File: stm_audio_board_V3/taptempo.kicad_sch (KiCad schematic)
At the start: 19 parts, among them J17 Conn_01x10_Footswitch, U13 74HC14

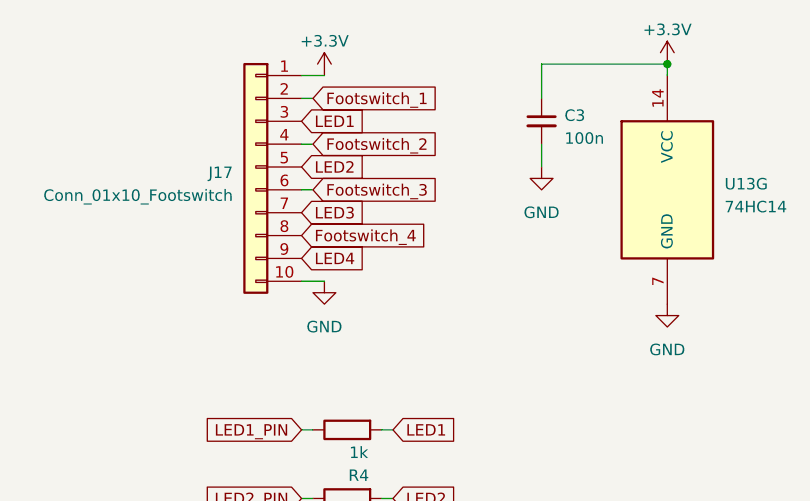
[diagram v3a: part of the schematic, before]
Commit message: added external pot, added feedback leds, added I2C between MCUs
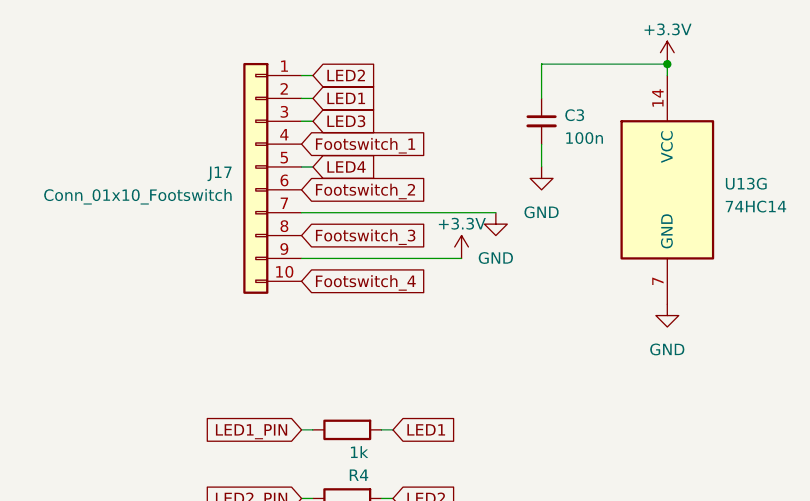
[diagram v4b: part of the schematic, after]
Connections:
- net +3.3V: now also J17.9 (Pin_9); no longer J17.1 (Pin_1)
- net Footswitch_1: now also J17.4 (Pin_4); no longer J17.2 (Pin_2)
- net Footswitch_2: now also J17.6 (Pin_6); no longer J17.4 (Pin_4)
- net Footswitch_3: now also J17.8 (Pin_8); no longer J17.6 (Pin_6)
- net Footswitch_4: now also J17.10 (Pin_10); no longer J17.8 (Pin_8)
- net GND: now also J17.7 (Pin_7); no longer J17.10 (Pin_10)
- net LED1: now also J17.2 (Pin_2); no longer J17.3 (Pin_3)
- net LED2: now also J17.1 (Pin_1); no longer J17.5 (Pin_5)
- net LED3: now also J17.3 (Pin_3); no longer J17.7 (Pin_7)
- net LED4: now also J17.5 (Pin_5); no longer J17.9 (Pin_9)

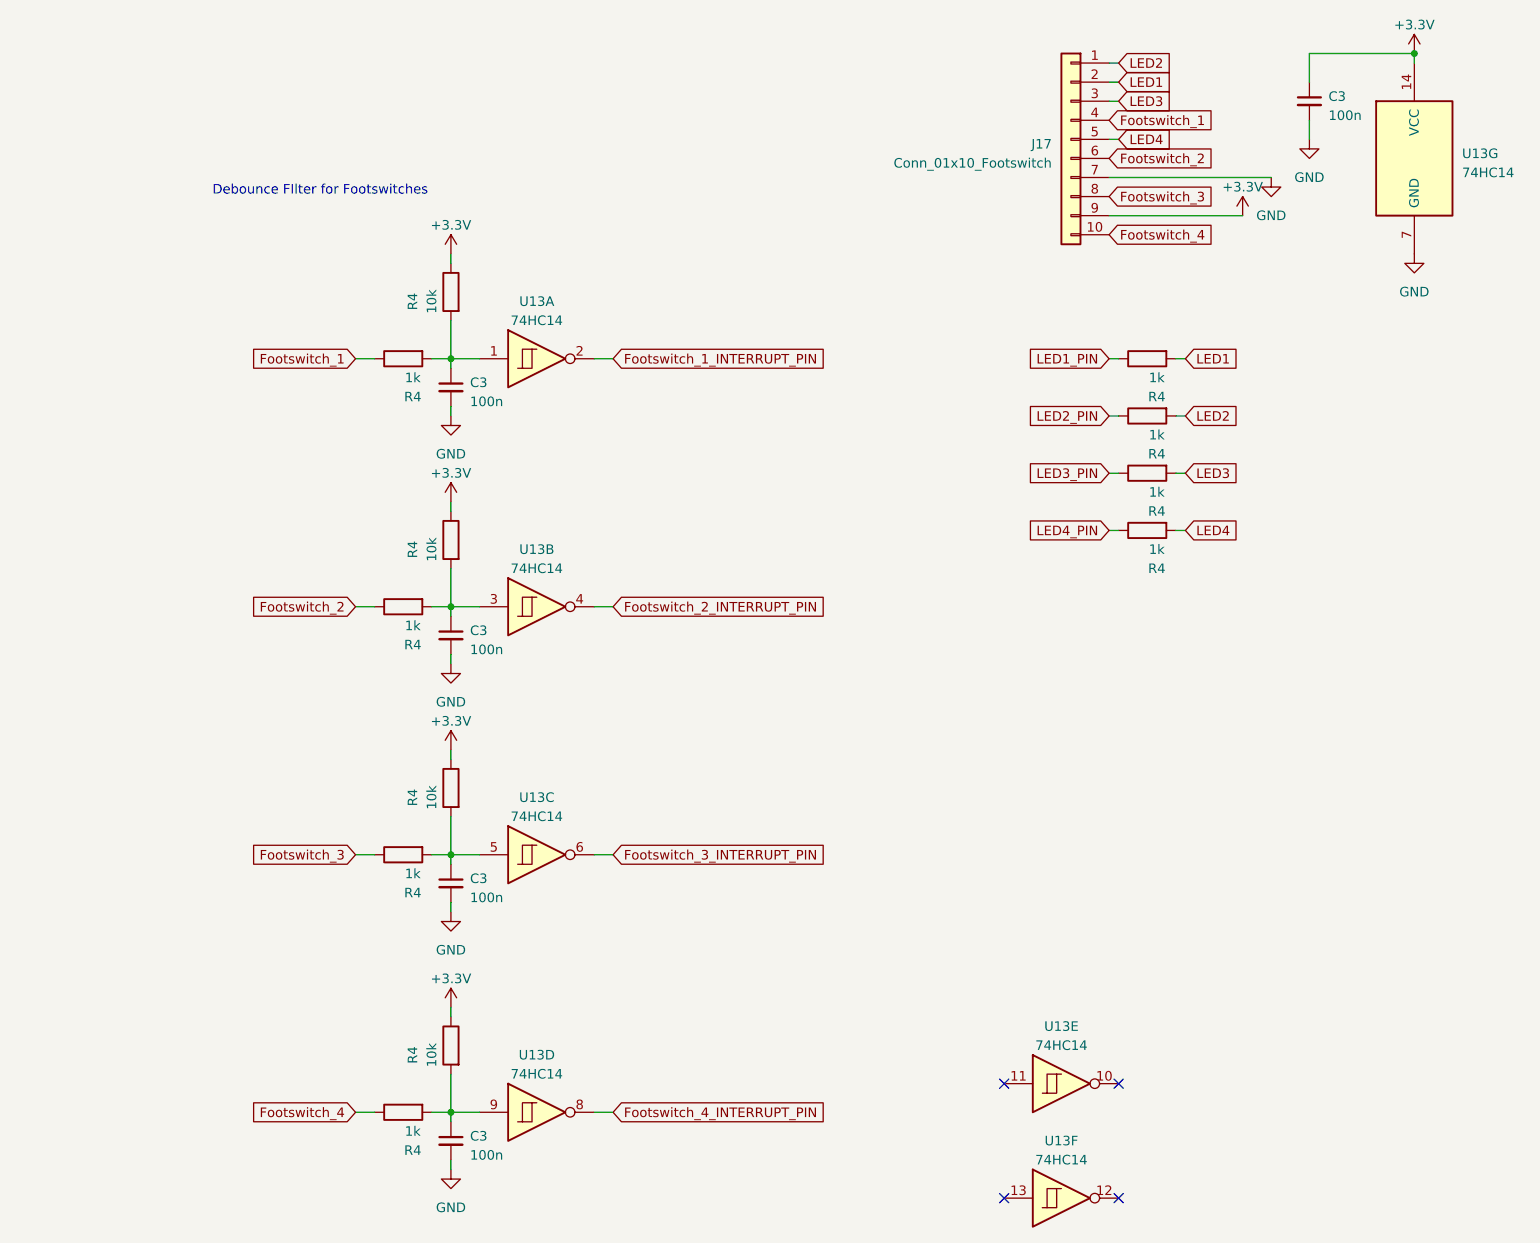
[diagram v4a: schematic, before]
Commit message: minor changes to components
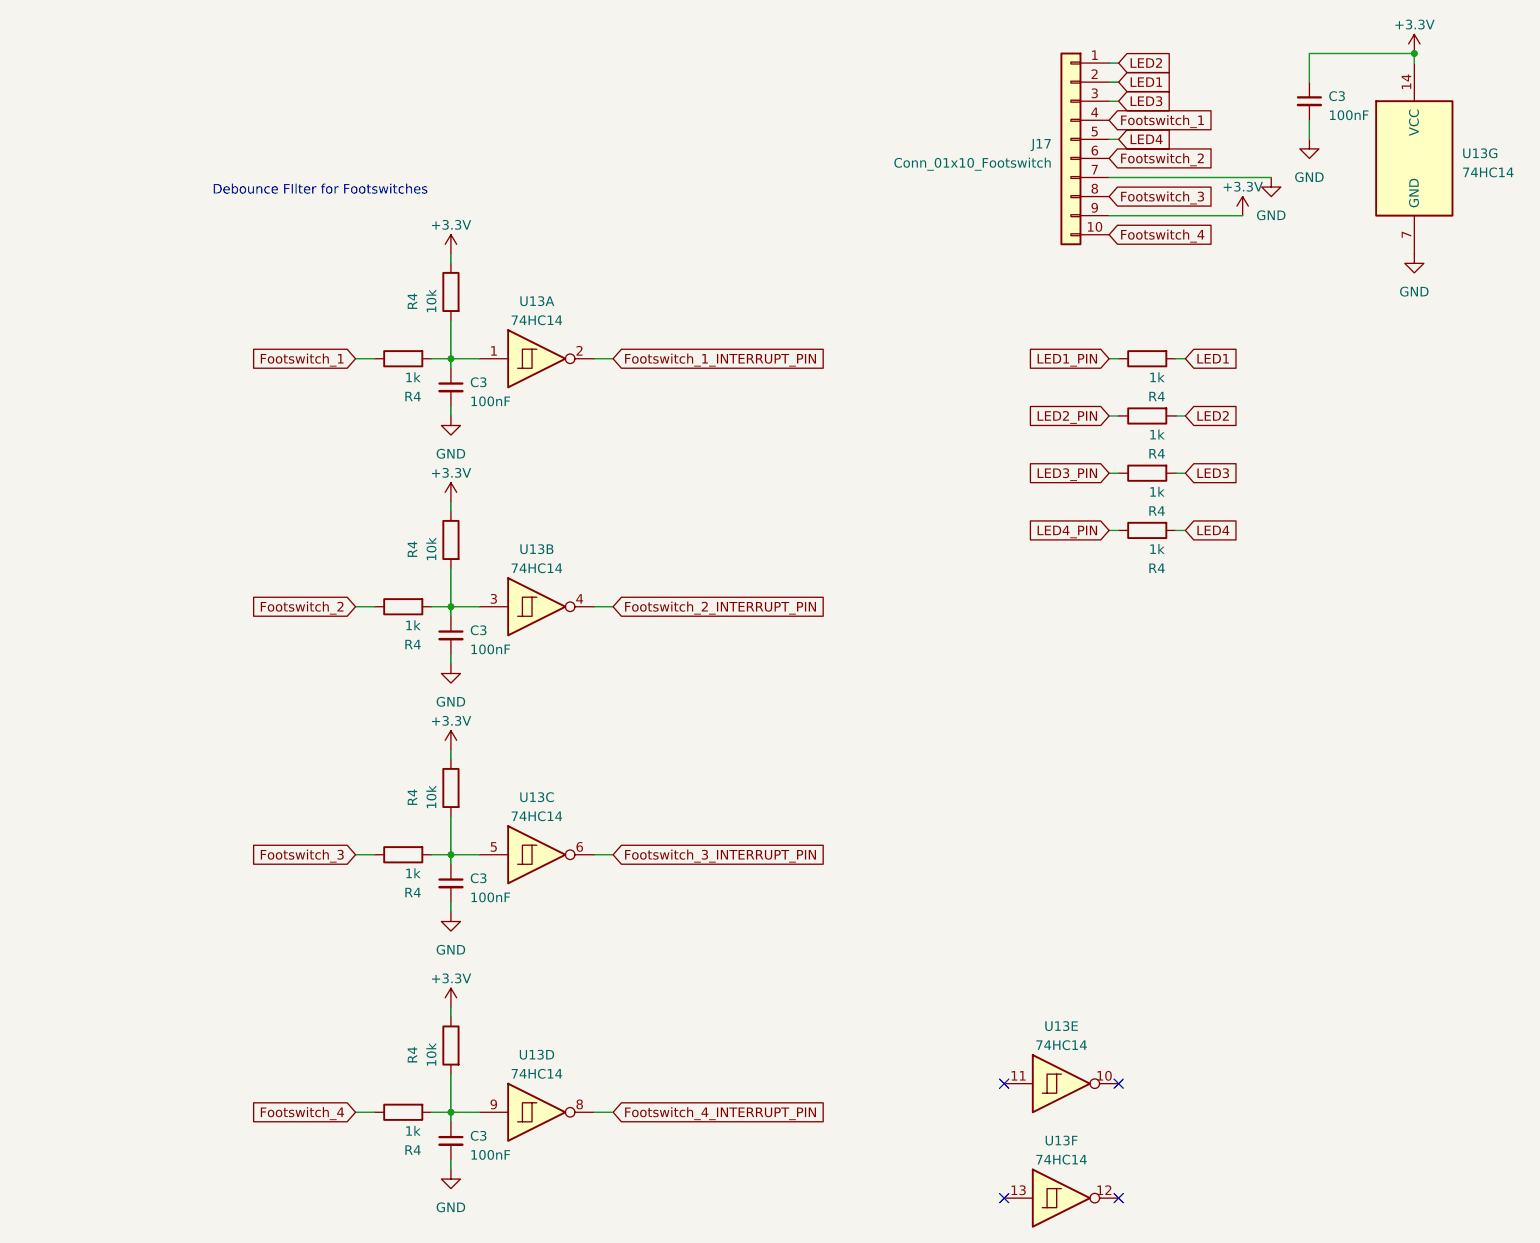
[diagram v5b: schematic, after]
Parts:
- C3: value 100n -> 100nF; JLCPCB (none) -> C14663; LCSC Part (none) -> C14663
- J17: LCSC Part (none) -> C5665
- R4: footprint Resistor_SMD:R_0603_1608Metric_Pad0.98x0.95mm_HandSolder -> Resistor_SMD:R_0603_1608Metric; JLCPCB (none) -> C21190; LCSC Part (none) -> C21190
- R4: footprint Resistor_SMD:R_0603_1608Metric_Pad0.98x0.95mm_HandSolder -> Resistor_SMD:R_0603_1608Metric; JLCPCB (none) -> C25804; LCSC Part (none) -> C25804
- U13: LCSC Part (none) -> C5605
